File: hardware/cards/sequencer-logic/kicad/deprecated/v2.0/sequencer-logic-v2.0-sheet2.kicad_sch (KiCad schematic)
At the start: 9 parts, among them IC13 74*374, IC14 74*374, IC15 74*374, IC16 74*374, IC17 74*374, IC18 74*374, IC19 74*374, IC20 74*374

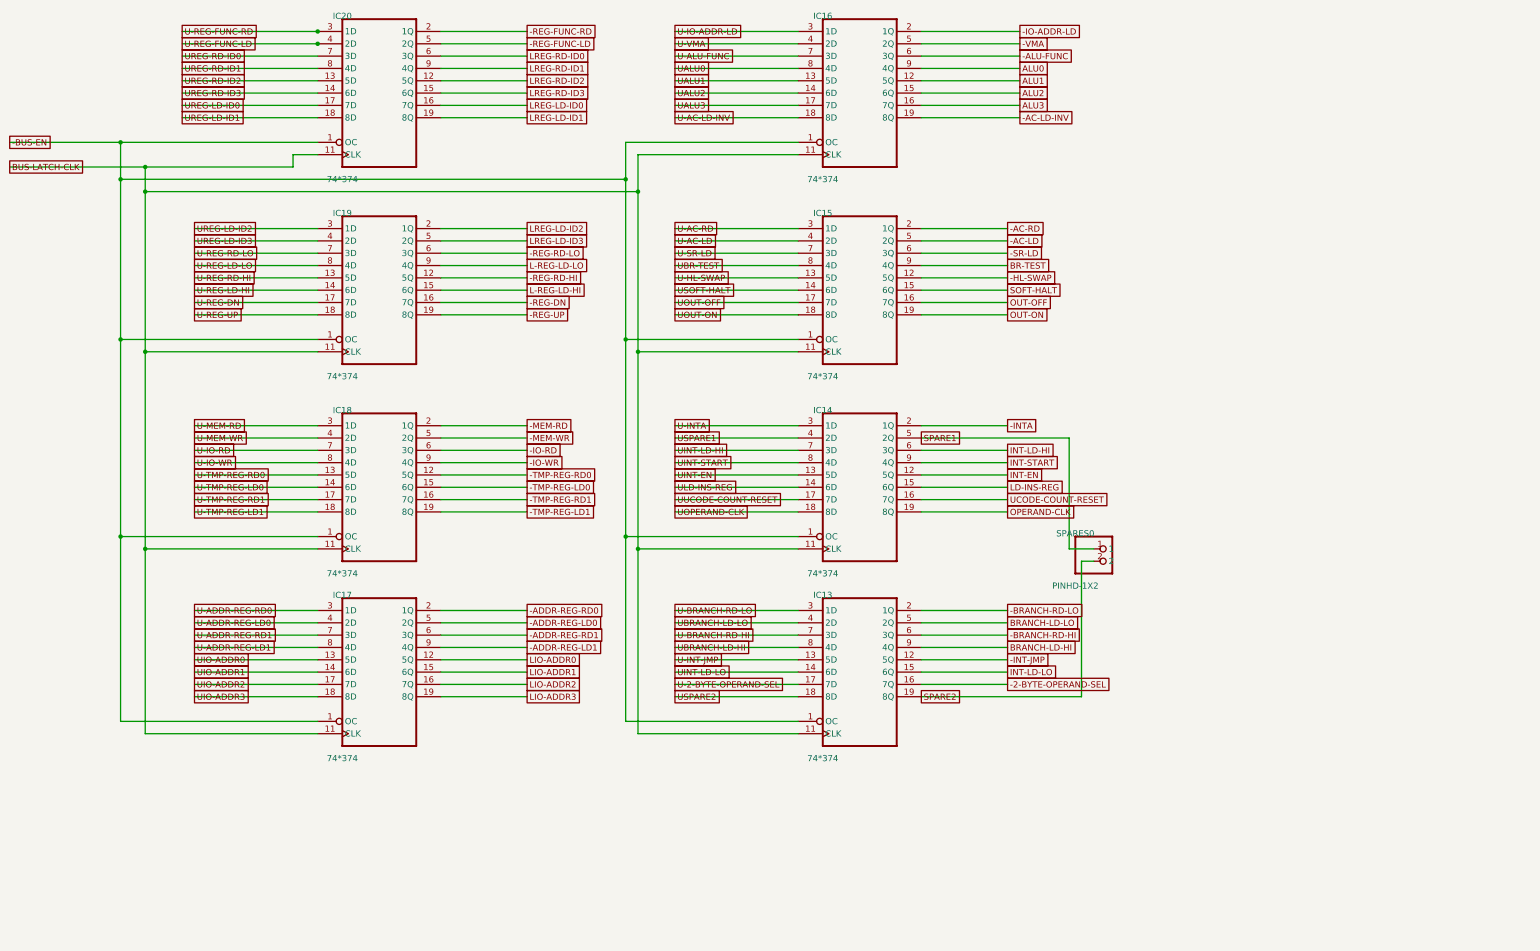
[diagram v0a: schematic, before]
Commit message: fix(kicad): readable converted schematics - overlaps 42,847 -> 3,147, nothing off the frame; CF sheet 0 overlaps
- tools/kicad/sch_overlaps.py: calibrated readability check (text/text, text/body, text/line, off frame/title block)
- eagle_sch_to_kicad.py: fields placed from Eagle's smashed attributes or the symbol's >NAME/>VALUE with Eagle's align,
  size and ratio, readable angles; fields Eagle never shows hidden (FABC96R shows only its pin name); pin numbers hidden
  where every Eagle pin hides them; Eagle-hidden layers dropped (the stray SpiceOrder text); labels on their own wires,
  converter labels only where KiCad needs them; rotate-then-mirror fixed for MR90/MR270 in pin_world/no-connects;
  each sheet on the smallest page that holds it, centred clear of the title block
- finish_board.py: stable footprint-library choice (DRC counts no longer vary run to run)
- all 37 projects regenerated: netlist proofs unchanged (34 MATCH, 2 schematic-only, video Fusion export MISMATCH as
  before); DRC same or better; ERC up (loose wire ends onto graphic buses no longer hidden by labels; explained per README)
- CF card: gate names off the gate bodies, U3 clear of its title, 5.08 mm connector pins; rebuilt: DRC 0/0, proof MATCH
- schematic PDFs regenerated (tools/sch_to_pdf.py, 37/37)

Co-Authored-By: Claude Opus 5.5 <noreply@anthropic.com>
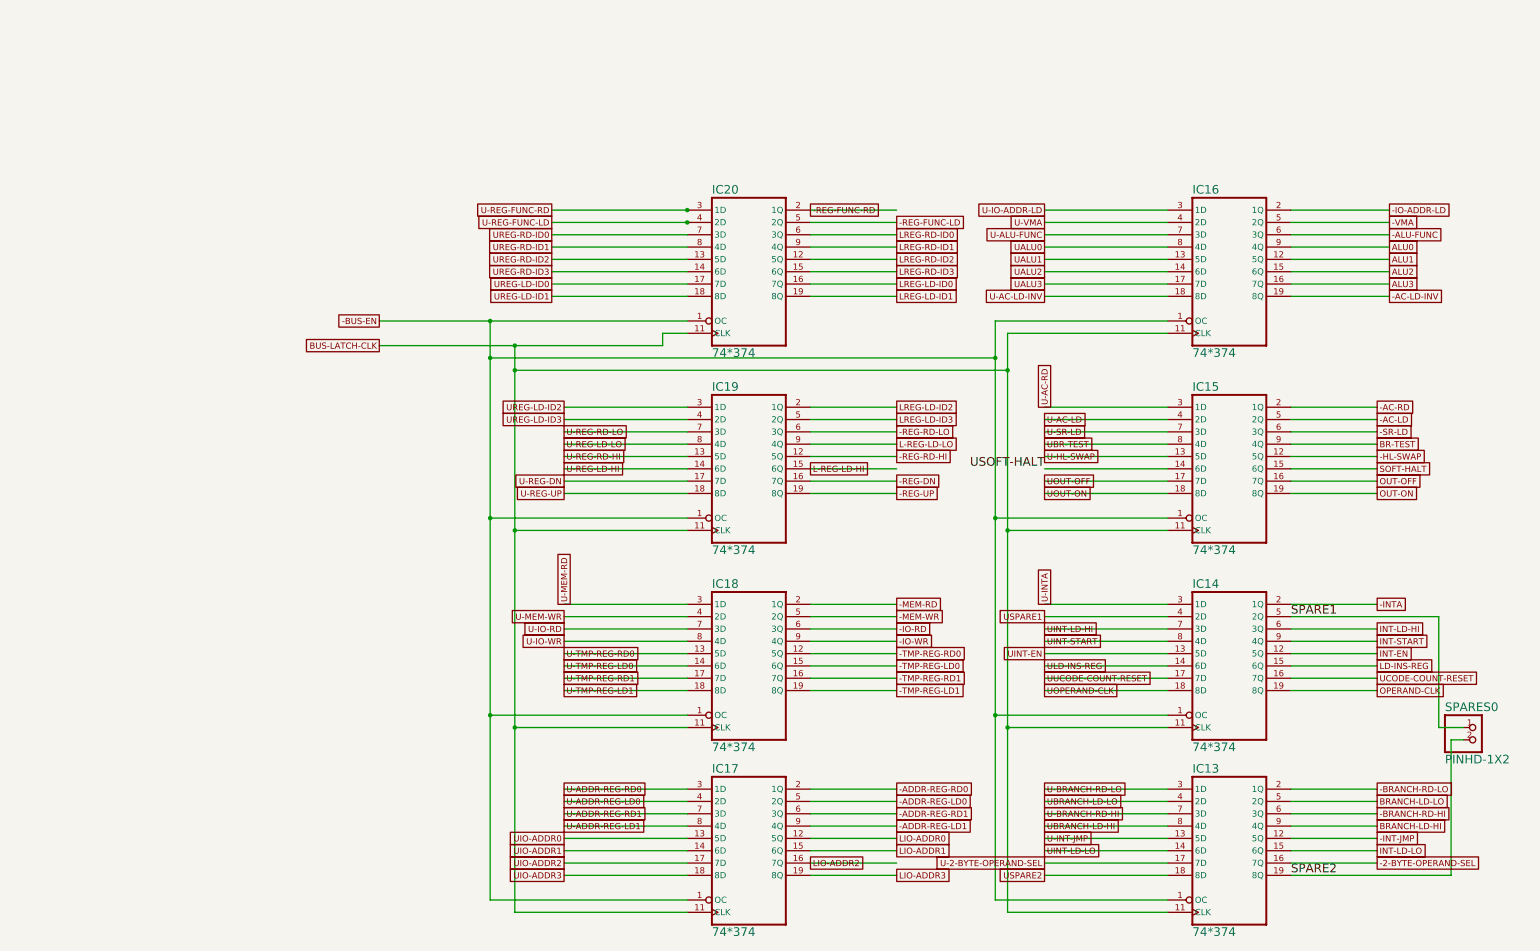
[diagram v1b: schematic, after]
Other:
- moved on the sheet: IC13, IC14, IC15, IC16, IC17, IC18, IC19, IC20
